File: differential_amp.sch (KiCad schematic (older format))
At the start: 16 parts, among them J1 RJ45, P1 CON, P2 gnd_ref, U1 AD8422, U2 AD8609

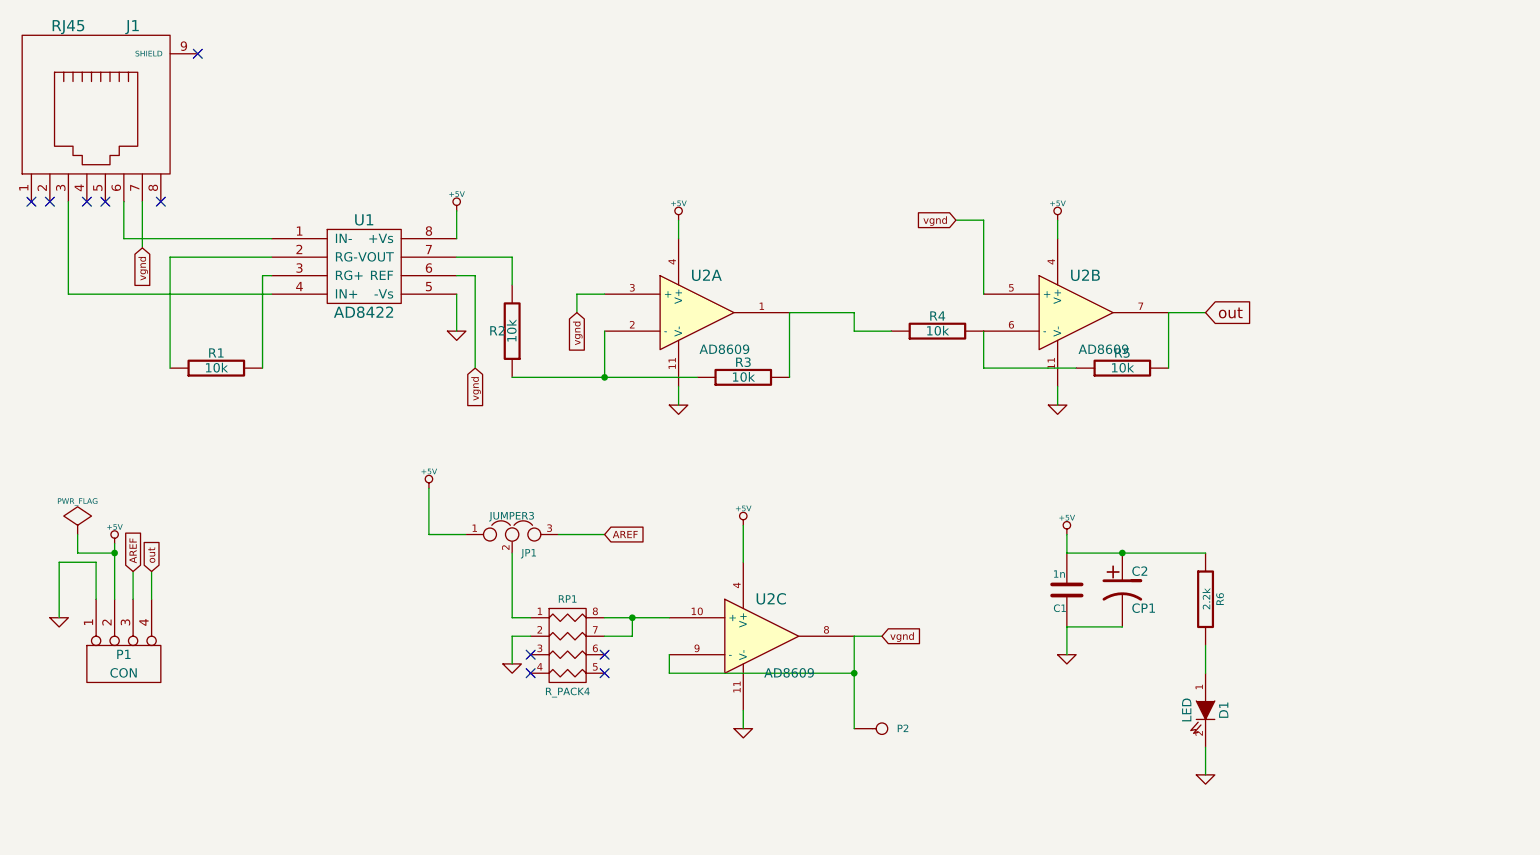
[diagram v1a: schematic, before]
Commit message: Added gain selection and 5v output on rj45
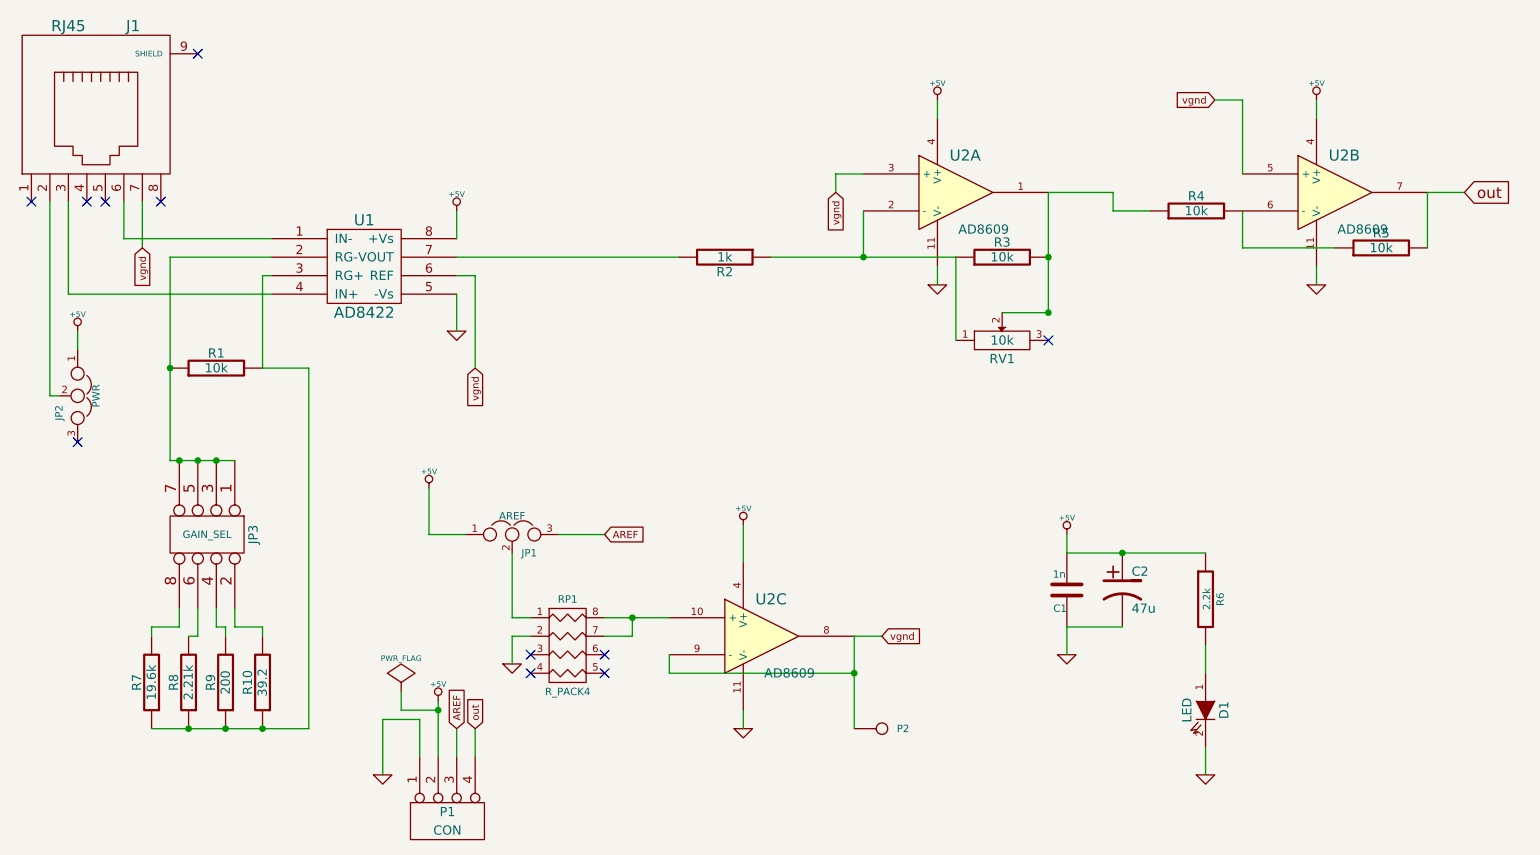
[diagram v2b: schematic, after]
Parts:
- added JP2: PWR, ~, symbol JUMPER3
- added JP3: GAIN_SEL, symbol CONN_4X2
- added R10: 39.2, symbol R
- added R7: 19.6k, symbol R
- added R8: 2.21k, symbol R
- added R9: 200, symbol R
- added RV1: 10k, ~, symbol POT
- C2: value CP1 -> 47u
- JP1: value JUMPER3 -> AREF
- R2: value 10k -> 1k
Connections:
- net +5V: now also JP2.1
- net at R1.1, U1.2 (RG-): now also JP3.1, JP3.3, JP3.5, JP3.7
- net at R1.2, U1.3 (RG+): now also R10.1, R7.1, R8.1, R9.1
- net at R3.2, R4.1, U2.1: now also RV1.2
- net at R2.1, R3.1, U2.2 (-): now also RV1.1
- net at J1.2: now also JP2.2
- new net: JP3.2, R10.2
- new net: JP3.4, R9.2
- new net: JP3.6, R8.2
- new net: JP3.8, R7.2
- no-connect marks 10 -> 11
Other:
- moved on the sheet: P1, R2, R3, R4, R5, U2A, U2B

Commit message: Removed rj45, added multiturn pot
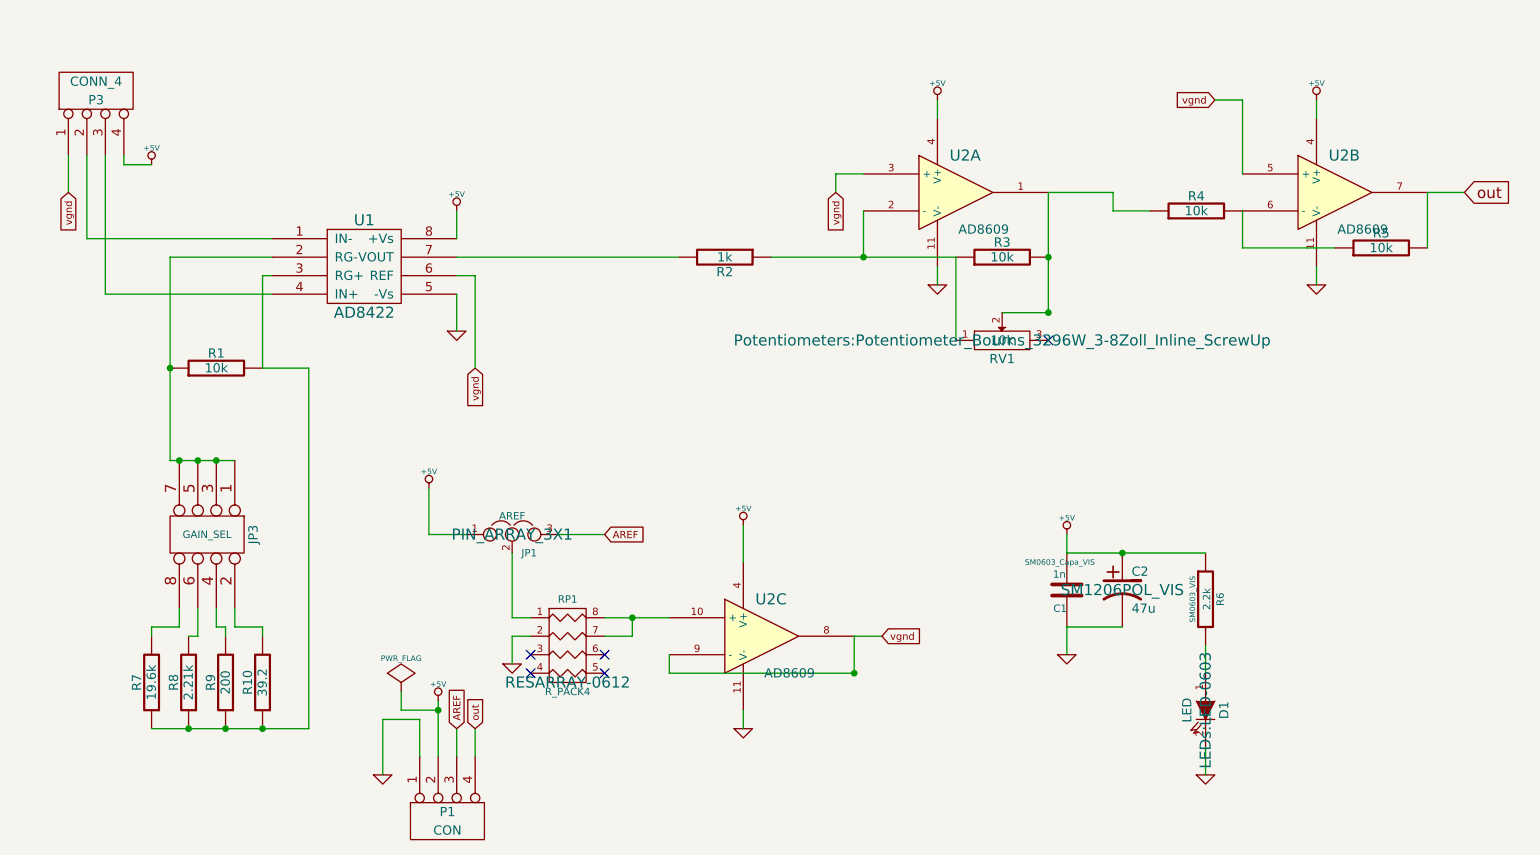
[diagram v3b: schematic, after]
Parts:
- removed J1: RJ45, symbol RJ45
- removed JP2: PWR, ~, symbol JUMPER3
- removed P2: gnd_ref, symbol CONN_1
- added P3: CONN_4, Connect:bornier4, symbol CONN_4
- C1: footprint ~ -> SM0603_Capa_VIS
- C2: footprint ~ -> SM1206POL_VIS
- D1: footprint ~ -> LEDs:LED-0603
- JP1: footprint ~ -> PIN_ARRAY_3X1
- JP3: footprint (none) -> pin_array_4x2
- P1: footprint (none) -> Connect:bornier4
- R1, R10, R2, R3, R4, R5, R7, R8, R9: footprint (none) -> SM0603_VIS
- R6: footprint ~ -> SM0603_VIS
- RP1: footprint ~ -> RESARRAY-0612
- RV1: footprint ~ -> Potentiometers:Potentiometer_Bourns_3296W_3-8Zoll_Inline_ScrewUp
- U1: footprint (none) -> SO8E
- U2: footprint (none) -> SO14E
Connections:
- net +5V: now also P3.4 (P4)
- net vgnd: now also P3.1 (P1)
- net at U1.1 (IN-): now also P3.2 (P2)
- net at U1.4 (IN+): now also P3.3 (P3)
- no-connect marks 11 -> 5
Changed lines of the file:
@@
 LIBS:visgence_parts
 LIBS:differential_amp-cache
-EELAYER 27 0
+EELAYER 24 0
 EELAYER END
 $Descr USLetter 11000 8500
@@
 F 0 "U1" H 2900 2250 60  0000 C CNN
 F 1 "AD8422" H 2900 1750 60  0000 C CNN
-F 2 "" H 2900 2000 60  0001 C CNN
+F 2 "SO8E" H 2900 2000 60  0001 C CNN
 F 3 "" H 2900 2000 60  0001 C CNN
 	1    2900 2000
@@
 F 0 "R5" V 8480 1900 50  0000 C CNN
 F 1 "10k" V 8400 1900 50  0000 C CNN
-F 2 "" H 8400 1900 60  0001 C CNN
+F 2 "SM0603_VIS" H 8400 1900 60  0001 C CNN
 F 3 "" H 8400 1900 60  0001 C CNN
 	1    8400 1900
@@
 F 0 "R4" V 7480 1700 50  0000 C CNN
 F 1 "10k" V 7400 1700 50  0000 C CNN
-F 2 "" H 7400 1700 60  0001 C CNN
+F 2 "SM0603_VIS" H 7400 1700 60  0001 C CNN
 F 3 "" H 7400 1700 60  0001 C CNN
 	1    7400 1700
@@
 F 0 "R3" V 6430 1950 50  0000 C CNN
 F 1 "10k" V 6350 1950 50  0000 C CNN
-F 2 "" H 6350 1950 60  0001 C CNN
+F 2 "SM0603_VIS" H 6350 1950 60  0001 C CNN
 F 3 "" H 6350 1950 60  0001 C CNN
 	1    6350 1950
@@
 F 0 "R2" V 4930 1950 50  0000 C CNN
 F 1 "1k" V 4850 1950 50  0000 C CNN
-F 2 "" H 4850 1950 60  0001 C CNN
+F 2 "SM0603_VIS" H 4850 1950 60  0001 C CNN
 F 3 "" H 4850 1950 60  0001 C CNN
 	1    4850 1950
@@
 	4550 4200 5550 4200
 Wire Wire Line
-	5550 4000 5550 4500
-Wire Wire Line
 	4950 4400 4950 4500
 $Comp
@@
 F 0 "U2" H 5100 4200 60  0000 C CNN
 F 1 "AD8609" H 5200 3800 50  0000 C CNN
-F 2 "" H 5050 4000 60  0000 C CNN
+F 2 "SO14E" H 5050 4000 60  0001 C CNN
 F 3 "" H 5050 4000 60  0000 C CNN
 	3    5050 4000
@@
 F 0 "U2" H 6150 1800 60  0000 C CNN
 F 1 "AD8609" H 6250 1400 50  0000 C CNN
-F 2 "" H 6100 1600 60  0000 C CNN
+F 2 "SO14E" H 6100 1600 60  0001 C CNN
 F 3 "" H 6100 1600 60  0000 C CNN
 	1    6100 1600
@@
 F 0 "U2" H 8200 1800 60  0000 C CNN
 F 1 "AD8609" H 8300 1400 50  0000 C CNN
-F 2 "" H 8150 1600 60  0000 C CNN
+F 2 "SO14E" H 8150 1600 60  0001 C CNN
 F 3 "" H 8150 1600 60  0000 C CNN
 	2    8150 1600
@@
 F 0 "C1" H 6700 3850 40  0000 L CNN
 F 1 "1n" H 6706 3665 40  0000 L CNN
-F 2 "~" H 6738 3600 30  0000 C CNN
+F 2 "SM0603_Capa_VIS" H 6738 3600 30  0000 C CNN
 F 3 "~" H 6700 3750 60  0000 C CNN
 	1    6700 3750
@@
 F 0 "C2" H 7050 3850 50  0000 L CNN
 F 1 "47u" H 7050 3650 50  0000 L CNN
-F 2 "~" H 7000 3750 60  0000 C CNN
+F 2 "SM1206POL_VIS" H 7000 3750 60  0000 C CNN
 F 3 "~" H 7000 3750 60  0000 C CNN
 	1    7000 3750
@@
 F 0 "R6" V 7530 3800 40  0000 C CNN
 F 1 "2.2k" V 7457 3801 40  0000 C CNN
-F 2 "~" V 7380 3800 30  0000 C CNN
+F 2 "SM0603_VIS" V 7380 3800 30  0000 C CNN
 F 3 "~" H 7450 3800 30  0000 C CNN
 	1    7450 3800
@@
 F 0 "D1" H 7450 4500 50  0000 C CNN
 F 1 "LED" H 7450 4300 50  0000 C CNN
-F 2 "~" H 7450 4400 60  0000 C CNN
+F 2 "LEDs:LED-0603" H 7450 4400 60  0000 C CNN
 F 3 "~" H 7450 4400 60  0000 C CNN
 	1    7450 4400
@@
 Text GLabel 7500 1100 0    39   Input ~ 0
 vgnd
-$Comp
-L RJ45 J1
-U 1 1 53791EBC
-P 1450 1200
-F 0 "J1" H 1650 1700 60  0000 C CNN
-F 1 "RJ45" H 1300 1700 60  0000 C CNN
-F 2 "" H 1450 1200 60  0000 C CNN
-F 3 "" H 1450 1200 60  0000 C CNN
-	1    1450 1200
-	1    0    0    -1
-$EndComp
-Wire Wire Line
-	1300 1650 1300 2150
-Wire Wire Line
-	1300 2150 2400 2150
-Wire Wire Line
-	1600 1650 1600 1850
-Wire Wire Line
-	1600 1850 2400 1850
-Text GLabel 1700 1900 3    39   Input ~ 0
+Text GLabel 1300 1600 3    39   Input ~ 0
 vgnd
-Wire Wire Line
-	1700 1900 1700 1650
-NoConn ~ 1100 1650
-NoConn ~ 1400 1650
-NoConn ~ 1500 1650
-NoConn ~ 1800 1650
 $Comp
 L R R1
@@
 F 0 "R1" V 2180 2550 50  0000 C CNN
 F 1 "10k" V 2100 2550 50  0000 C CNN
-F 2 "" H 2100 2550 60  0001 C CNN
+F 2 "SM0603_VIS" H 2100 2550 60  0001 C CNN
 F 3 "" H 2100 2550 60  0001 C CNN
 	1    2100 2550
@@
 F 0 "RP1" H 4000 4700 40  0000 C CNN
 F 1 "R_PACK4" H 4000 4200 40  0000 C CNN
-F 2 "~" H 4000 4250 60  0000 C CNN
+F 2 "RESARRAY-0612" H 4000 4250 60  0000 C CNN
 F 3 "~" H 4000 4250 60  0000 C CNN
 	1    4000 4250
@@
 F 0 "JP1" H 3750 3350 40  0000 L CNN
 F 1 "AREF" H 3700 3550 40  0000 C CNN
-F 2 "~" H 3700 3450 60  0000 C CNN
+F 2 "PIN_ARRAY_3X1" H 3700 3450 60  0000 C CNN
 F 3 "~" H 3700 3450 60  0000 C CNN
 	1    3700 3450
@@
 Wire Wire Line
 	3950 3450 4200 3450
-$Comp
-L CONN_1 P2
-U 1 1 5379257B
-P 5700 4500
-F 0 "P2" H 5780 4500 40  0000 L CNN
-F 1 "gnd_ref" H 5700 4555 30  0001 C CNN
-F 2 "" H 5700 4500 60  0000 C CNN
-F 3 "" H 5700 4500 60  0000 C CNN
-	1    5700 4500
-	1    0    0    -1
-$EndComp
 Connection ~ 5550 4200
 $Comp
@@
 F 0 "P1" V 3300 5000 50  0000 C CNN
 F 1 "CON" V 3400 5000 50  0000 C CNN
-F 2 "" H 3350 5000 60  0000 C CNN
+F 2 "Connect:bornier4" H 3350 5000 60  0001 C CNN
 F 3 "" H 3350 5000 60  0000 C CNN
 	1    3350 5000
@@
 Wire Wire Line
 	3500 4650 3500 4500
-NoConn ~ 2000 850
 Wire Wire Line
 	5600 1700 5600 1950
@@
 F 0 "JP3" H 2050 3700 50  0000 C CNN
 F 1 "GAIN_SEL" V 2050 3450 40  0000 C CNN
-F 2 "" H 2050 3450 60  0000 C CNN
+F 2 "pin_array_4x2" H 2050 3450 60  0001 C CNN
 F 3 "" H 2050 3450 60  0000 C CNN
 	1    2050 3450
@@
 F 0 "R7" V 1830 4250 50  0000 C CNN
 F 1 "19.6k" V 1750 4250 50  0000 C CNN
-F 2 "" H 1750 4250 60  0001 C CNN
+F 2 "SM0603_VIS" H 1750 4250 60  0001 C CNN
 F 3 "" H 1750 4250 60  0001 C CNN
 	1    1750 4250
@@
 F 0 "R8" V 2030 4250 50  0000 C CNN
 F 1 "2.21k" V 1950 4250 50  0000 C CNN
-F 2 "" H 1950 4250 60  0001 C CNN
+F 2 "SM0603_VIS" H 1950 4250 60  0001 C CNN
 F 3 "" H 1950 4250 60  0001 C CNN
 	1    1950 4250
@@
 F 0 "R9" V 2230 4250 50  0000 C CNN
 F 1 "200" V 2150 4250 50  0000 C CNN
-F 2 "" H 2150 4250 60  0001 C CNN
+F 2 "SM0603_VIS" H 2150 4250 60  0001 C CNN
 F 3 "" H 2150 4250 60  0001 C CNN
 	1    2150 4250
@@
 F 0 "R10" V 2430 4250 50  0000 C CNN
 F 1 "39.2" V 2350 4250 50  0000 C CNN
-F 2 "" H 2350 4250 60  0001 C CNN
+F 2 "SM0603_VIS" H 2350 4250 60  0001 C CNN
 F 3 "" H 2350 4250 60  0001 C CNN
 	1    2350 4250
@@
 F 0 "RV1" H 6350 2300 50  0000 C CNN
 F 1 "10k" H 6350 2400 50  0000 C CNN
-F 2 "~" H 6350 2400 60  0000 C CNN
+F 2 "Potentiometers:Potentiometer_Bourns_3296W_3-8Zoll_Inline_ScrewUp" H 6350 2400 60  0000 C CNN
 F 3 "~" H 6350 2400 60  0000 C CNN
 	1    6350 2400
@@
 	3400 1950 4600 1950
 $Comp
-L JUMPER3 JP2
-U 1 1 5389543C
-P 1350 2700
-F 0 "JP2" H 1400 2600 40  0000 L CNN
-F 1 "PWR" H 1350 2800 40  0000 C CNN
-F 2 "~" H 1350 2700 60  0000 C CNN
-F 3 "~" H 1350 2700 60  0000 C CNN
-	1    1350 2700
-	0    1    1    0
-$EndComp
-Wire Wire Line
-	1200 1650 1200 2700
-Wire Wire Line
-	1200 2700 1250 2700
-$Comp
 L +5V #PWR017
 U 1 1 538955E2
-P 1350 2350
-F 0 "#PWR017" H 1350 2440 20  0001 C CNN
-F 1 "+5V" H 1350 2440 30  0000 C CNN
-F 2 "" H 1350 2350 60  0000 C CNN
-F 3 "" H 1350 2350 60  0000 C CNN
-	1    1350 2350
-	1    0    0    -1
-$EndComp
-Wire Wire Line
-	1350 2350 1350 2450
-NoConn ~ 1350 2950
+P 1750 1450
+F 0 "#PWR017" H 1750 1540 20  0001 C CNN
+F 1 "+5V" H 1750 1540 30  0000 C CNN
+F 2 "" H 1750 1450 60  0000 C CNN
+F 3 "" H 1750 1450 60  0000 C CNN
+	1    1750 1450
+	1    0    0    -1
+$EndComp
+$Comp
+L CONN_4 P3
+U 1 1 53F1B25C
+P 1450 1050
+F 0 "P3" V 1400 1050 50  0000 C CNN
+F 1 "CONN_4" V 1500 1050 50  0000 C CNN
+F 2 "Connect:bornier4" H 1450 1050 60  0001 C CNN
+F 3 "" H 1450 1050 60  0000 C CNN
+	1    1450 1050
+	0    -1   -1   0
+$EndComp
+Wire Wire Line
+	1300 1600 1300 1400
+Wire Wire Line
+	1750 1450 1600 1450
+Wire Wire Line
+	1600 1450 1600 1400
+Wire Wire Line
+	2400 1850 1400 1850
+Wire Wire Line
+	1400 1850 1400 1400
+Wire Wire Line
+	1500 1400 1500 2150
+Wire Wire Line
+	1500 2150 2400 2150
+Wire Wire Line
+	5550 4200 5550 4000
 $EndSCHEMATC
